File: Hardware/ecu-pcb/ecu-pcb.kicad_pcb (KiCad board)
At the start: 2 copper layers, 187 parts, among them CN1 B2B-XH-A(LF)(SN), CN10 B3B-PH-K-S(LF)(SN), CN2 B2B-XH-A(LF)(SN), CN3 0430450400, CN4 B3B-PH-K-S(LF)(SN), CN5 B2B-XH-A(LF)(SN), CN6 B3B-PH-K-S(LF)(SN), CN7 B2B-XH-A(LF)(SN), CN8 B2B-XH-A(LF)(SN), CN9 B2B-XH-A(LF)(SN)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

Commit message: PCB Done
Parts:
- removed F2, F3, F4, F5: 33V 750mA Fuse, easyeda2kicad:F1812
- removed LED5, LED7: Red LED 0603, easyeda2kicad:LED0603-R-RD
- removed R34: 1kΩ 0402 50V, easyeda2kicad:R0402
- removed TP4, TP7: TestPoint, TestPoint:TestPoint_Loop_D2.50mm_Drill1.0mm_LowProfile
- added CN11: B3B-PH-K-S(LF)(SN), easyeda2kicad:CONN-TH_B3B-PH-K-S, F.Cu at (122.2, 65.3)
- added D17: SMF05CT1G, easyeda2kicad:SOT-363_L2.0-W1.3-P0.65-LS2.1-BR, F.Cu at (120.5, 69.8)
- added D18: ZMM3V3, easyeda2kicad:LL-34_L3.5-W1.5-RD, F.Cu at (124.8, 69.3)
- added H1: MountingHole_3.2mm_M3_Pad_Via, MountingHole:MountingHole_3.2mm_M3_Pad_Via, F.Cu at (84.7, 58.6)
- added H2: MountingHole_3.2mm_M3_Pad_Via, MountingHole:MountingHole_3.2mm_M3_Pad_Via, F.Cu at (161.7, 58.6)
- added H3: MountingHole_3.2mm_M3_Pad_Via, MountingHole:MountingHole_3.2mm_M3_Pad_Via, F.Cu at (84.7, 126.6)
- added H4: MountingHole_3.2mm_M3_Pad_Via, MountingHole:MountingHole_3.2mm_M3_Pad_Via, F.Cu at (161.7, 126.6)
- added JP2: SolderJumper_3_Bridged12, Jumper:SolderJumper-3_P1.3mm_Bridged12_Pad1.0x1.5mm_NumberLabels, F.Cu at (127.6, 74.3)
- added L19: 100Ω 800mA, easyeda2kicad:L0805, F.Cu at (119.7, 74.3)
- C12, C32: value 100nF -> 10uF; footprint easyeda2kicad:C0402_NEW -> easyeda2kicad:C0402
- CN2: value B2B-XH-A(LF)(SN) -> B3B-PH-K-S(LF)(SN); footprint easyeda2kicad:CONN-TH_B2B-XH-A-LF-SN -> easyeda2kicad:CONN-TH_B3B-PH-K-S
- R14: value 1kΩ 0402 50V -> 100Ω 0402 50V
- R24: value 1kΩ 0402 50V -> 2.2kΩ 0402 50V
- moved R36 149.3 mm to (95.1, 128.7), turned to -90 degrees
- moved CN7 136.4 mm to (92.7, 123.5), turned to -90 degrees
- moved LED8 133.3 mm to (92.5, 128.7)
- moved Q5 131.0 mm to (101.2, 122.1), turned to -90 degrees
- moved D12 129.1 mm to (97.9, 123.5), turned to -90 degrees
- moved C44 128.5 mm to (118.9, 91.5), turned to 180 degrees
- moved R24 128.2 mm to (107.7, 105.4)
- moved L12 128.0 mm to (119.1, 94.3), turned to 180 degrees
- moved R37 126.9 mm to (101.9, 124.9), turned to 180 degrees
- moved C42 126.4 mm to (121.7, 93.0), turned to -90 degrees
- moved R23 125.8 mm to (119.8, 86.9), turned to 180 degrees
- moved R35 122.9 mm to (100.2, 125.4), turned to 90 degrees
- moved D6 120.0 mm to (119.3, 89.1), turned to -90 degrees
- moved CN4 117.6 mm to (120.7, 84.5)
- moved C46 115.1 mm to (126.0, 87.5)
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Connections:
- C12 pad 2: +3.3V -> Net-(C12-Pad2)
- C26 pad 2: +5V -> /Audio Amp/Vin_f
- C27 pad 2: +5V -> /Audio Amp/Vin_f
- C28 pad 2: +5V -> /Audio Amp/Vin_f
- C31 pad 1: +5V -> /Audio Amp/Vin_f
- C32 pad 2: +5V -> Net-(C32-Pad2)
- CN2 pad 1: Net-(CN2-Pad1) -> GND
- CN5 pad 1: Net-(CN5-Pad1) -> +12V
- CN7 pad 1: Net-(CN7-Pad1) -> +12V
- CN8 pad 1: Net-(CN8-Pad1) -> +12V
- CN9 pad 1: Net-(CN9-Pad1) -> +12V
- D12 pad 2: Net-(CN7-Pad1) -> +12V
- D13 pad 2: Net-(CN8-Pad1) -> +12V
- D14 pad 2: Net-(CN9-Pad1) -> +12V
- D16 pad 1: /Sensor Input/Sensor -> /IO35
- D2 pad 1: Net-(CN2-Pad1) -> Net-(D2-Pad1)
- D7 pad 2: Net-(CN5-Pad1) -> +12V
- L9 pad 2: +5V -> /Audio Amp/Vin_f
- R14 pad 1: Net-(LED3-Pad1) -> /IO34
- R14 pad 2: +12V -> Net-(CN11-Pad2)
- R24 pad 1: Net-(LED5-Pad1) -> +12V
- R24 pad 2: /APPS/Isolated Pot1/Apps_5v -> Net-(LED3-Pad1)
- R44 pad 1: /Sensor Input/Sensor -> /IO35
- R7 pad 1: Net-(CN2-Pad1) -> Net-(D2-Pad1)
- R8 pad 2: Net-(CN2-Pad1) -> Net-(D2-Pad1)
- U1 pad 6: unconnected-(U1-Pad6) -> /IO34
- U1 pad 7: unconnected-(U1-Pad7) -> /IO35
- U6 pad 2: +5V -> /Audio Amp/Vin_f
- U6 pad 3: +5V -> /Audio Amp/Vin_f
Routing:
- net GND: track 0.00 -> 222.1 mm, vias 0 -> 76
- net +5V: track 0.00 -> 164.9 mm, vias 0 -> 11
- net +12V: track 0.00 -> 107.7 mm, vias 0 -> 13
- net /IO12: track 0.00 -> 88.7 mm, vias 0 -> 2
- net /IO32: track 0.00 -> 82.4 mm
- net /IO26: track 0.00 -> 70.0 mm, vias 0 -> 2
- net /APPS2: track 0.00 -> 60.6 mm, vias 0 -> 1
- net /IO33: track 0.00 -> 60.3 mm, vias 0 -> 2
- net /IO35: track 0.00 -> 59.1 mm, vias 0 -> 2
- net /ESP_EN: track 0.00 -> 50.8 mm, vias 0 -> 2
- net /IO34: track 0.00 -> 49.8 mm, vias 0 -> 2
- net /CANR: track 0.00 -> 38.3 mm
- net /APPS1: track 0.00 -> 36.1 mm, vias 0 -> 1
- net +3.3V: track 0.00 -> 35.4 mm, vias 0 -> 12
- net /CAND: track 0.00 -> 31.1 mm, vias 0 -> 2
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- added copper zone on In2.Cu, net +12V
- added copper zone on In2.Cu, net +3.3V
- added copper zone on B.Cu, net GND
- added copper zone on F.Cu, net GND
- added copper zone on In1.Cu, net GND
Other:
- board outline added: 96.2 x 79.2 mm
- copper layers 2 -> 4
- board text added: "+ +"
- board text added: "+ S -"
- board text added: "- -"
- board text added: "12V Input"
- board text added: "12V TP"
- board text added: "3V3 LED"
- board text added: "3V3 TP"
- board text added: "5V TP"
- board text added: "APPS1 + S -"
- board text added: "APPS1 TP"
- board text added: "APPS2 + S -"
- board text added: "APPS2 TP"
- board text added: "CAN H L -"
- board text added: "Nextion + T R -"
- board text added: "Relay1 + -"
- board text added: "Relay2 + -"
- board text added: "Relay3 + -"
- board text added: "Relay4 + -"
- board text added: "Sensor 1"
- board text added: "Sensor 2"
- board text added: "Speaker + -"
- board text added: "USB PROG"

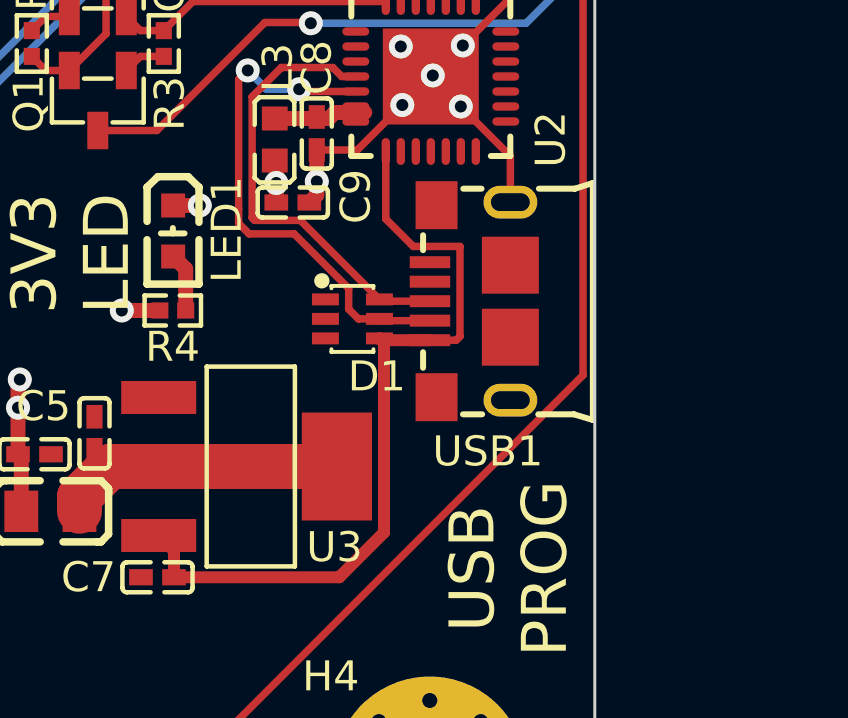
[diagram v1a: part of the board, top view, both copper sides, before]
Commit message: Added Vertical USB
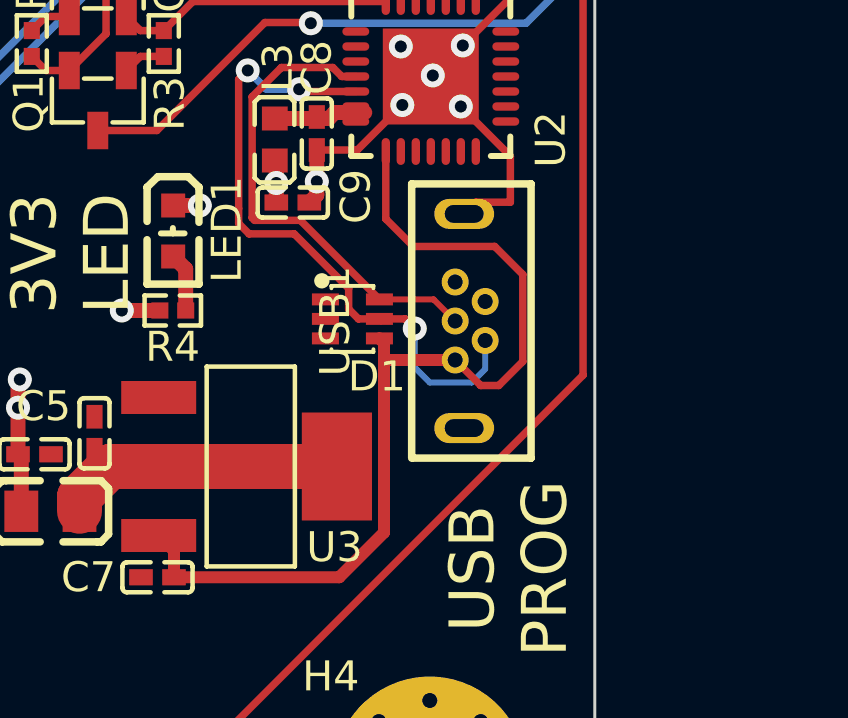
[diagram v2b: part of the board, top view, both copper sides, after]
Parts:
- USB1: value 10118193-0001LF -> U-E-M5DD-W-2; footprint easyeda2kicad:MICRO-USB-SMD_10118193-0001LF -> easyeda2kicad:MICRO-USB-TH_U-E-M5DD-W-2
- moved USB1 0.66 mm to (163.0, 111.5)
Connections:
- USB1 pad 7: (no net) -> GND
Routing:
- net /USB_CP2102/VBUS: track 26.6 -> 31.7 mm
- net /USB_CP2102/D-: track 17.2 -> 21.9 mm, vias 2 -> 3
- net GND: track 222.1 -> 223.8 mm
- net /USB_CP2102/D+: track 15.1 -> 16.3 mm
